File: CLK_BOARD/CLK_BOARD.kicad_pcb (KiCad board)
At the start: 4 copper layers, 46.5 x 38.7 mm, 79 parts, among them J1 PWR, J2 OUT_50M_1, J3 OUT_50M_2, J4 OUT_50M_3, J5 CTRL, J6 OUT_100M_3, J7 OUT_100M_2, J8 OUT_100M_1, U1 TPS7A9101DSKR, U2 LMK00804BQWRGTRQ1, U3 LMK00804BQWRGTRQ1, U4 SN74LVC1G74DCUR, X1 TB612-100.0M

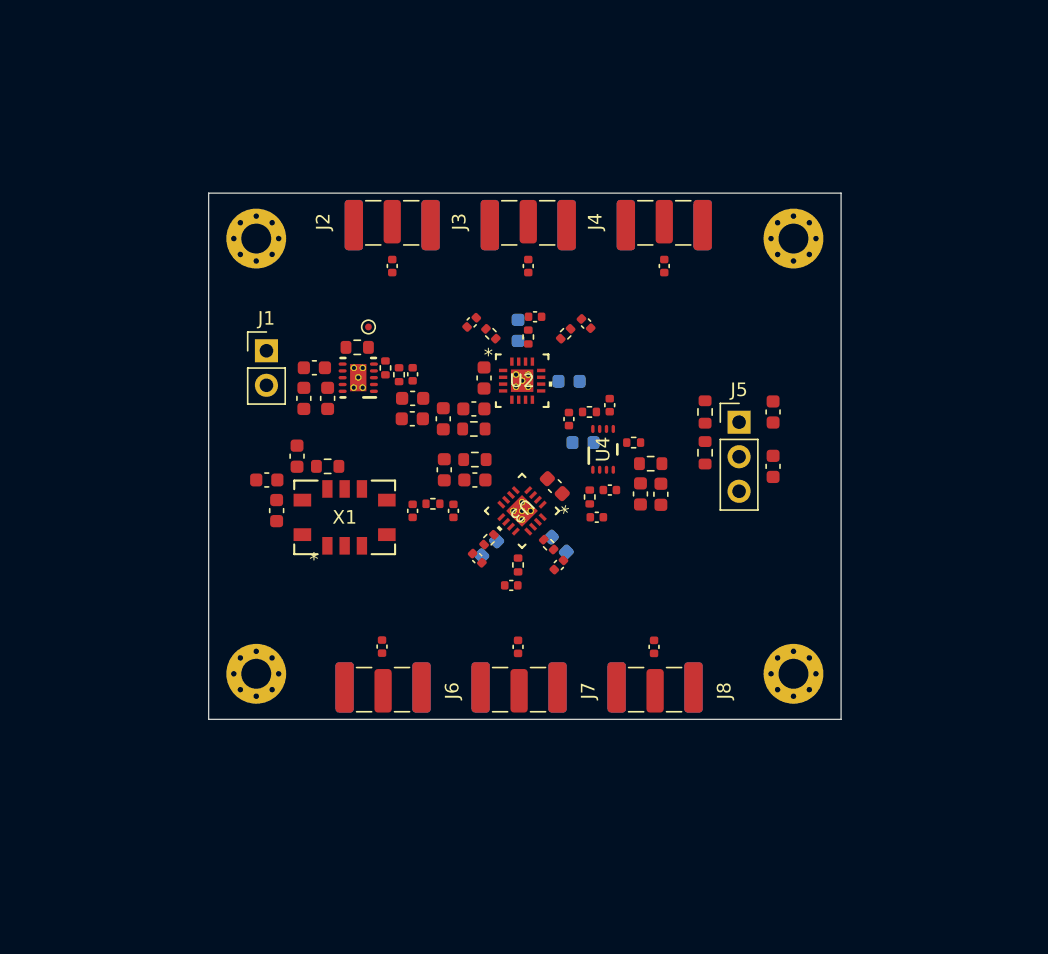
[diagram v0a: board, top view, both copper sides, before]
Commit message: component placement semi-final, and most tracks routed
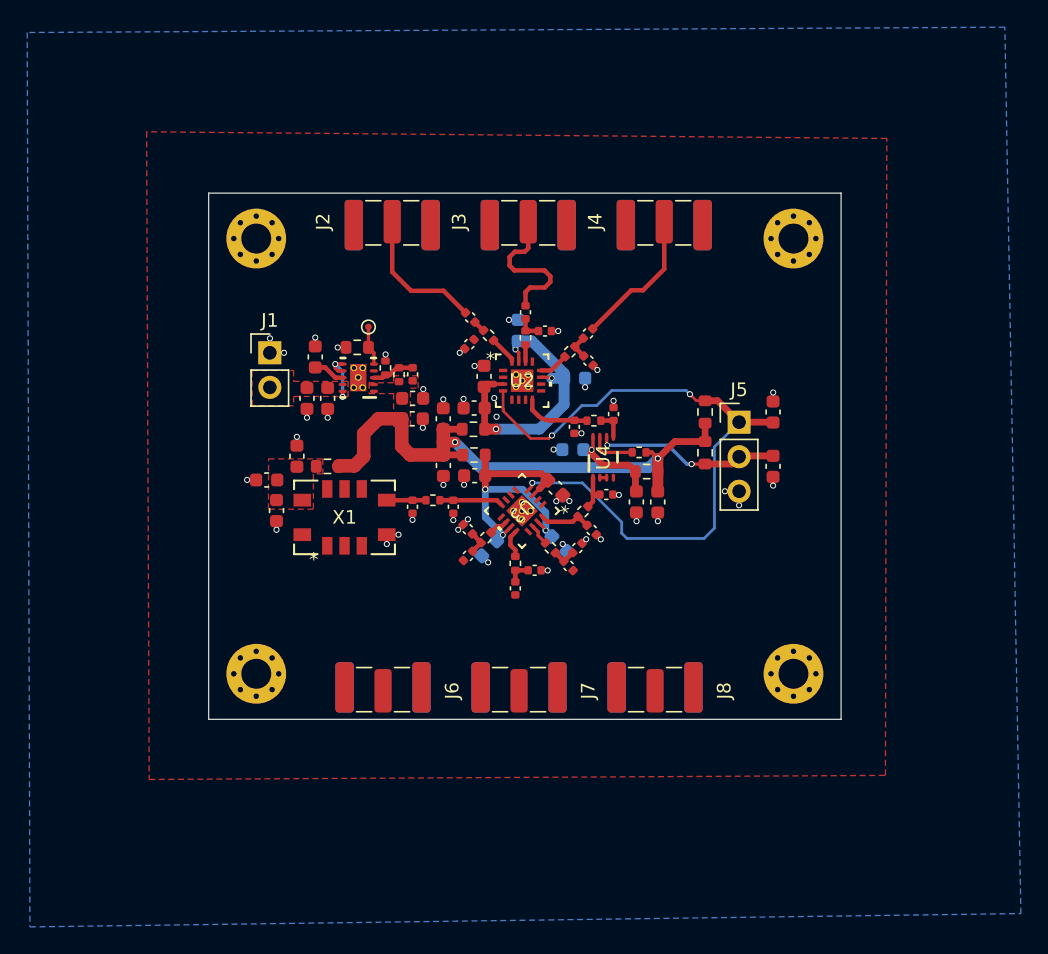
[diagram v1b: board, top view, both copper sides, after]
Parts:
- moved C35 9.19 mm to (131.1, 87.3), turned to -135 degrees
- moved C37 8.66 mm to (138.5, 88.1), turned to -45 degrees
- moved C28 7.49 mm to (139.9, 71.0), turned to -135 degrees
- moved C15 6.87 mm to (131.2, 69.8), turned to -45 degrees
- moved C36 4.30 mm to (134.6, 89.7)
- moved C22 3.41 mm to (135.3, 69.4)
- moved C29 2.73 mm to (139.9, 73.0)
- moved C32 2.24 mm to (131.1, 85.4), turned to 135 degrees
- moved C33 2.05 mm to (136.0, 88.4), turned to 0 degrees
- moved C34 1.85 mm to (139.1, 86.8), turned to 45 degrees
- moved C16 1.61 mm to (131.2, 71.8)
- moved R11 1.36 mm to (138.6, 72.3)
- moved C23 1.28 mm to (136.7, 70.8)
- moved R9 1.18 mm to (139.5, 84.1), turned to 45 degrees
- moved C24 1.01 mm to (140.2, 85.4), turned to -45 degrees
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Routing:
- net /nMUTE: track 0.00 -> 49.7 mm, vias 0 -> 3
- net +3V3: track 0.00 -> 42.8 mm, vias 0 -> 2
- net Net-(U3-VDD): track 0.00 -> 22.4 mm, vias 0 -> 3
- net Net-(U2-VDD): track 0.00 -> 21.3 mm, vias 0 -> 3
- net /nRST: track 0.00 -> 13.7 mm, vias 0 -> 2
- net Net-(J3-In): track 0.00 -> 11.1 mm
- net Net-(J4-In): track 0.00 -> 10.6 mm
- net Net-(J2-In): track 0.00 -> 10.3 mm
- net Net-(U4-VCC): track 0.00 -> 7.15 mm, vias 0 -> 1
- net Net-(U2-LVCMOS_CLK): track 0.00 -> 5.04 mm
- net /OSC_OUT: track 0.00 -> 4.65 mm
- net Net-(J1-Pin_2): track 0.00 -> 4.50 mm, vias 0 -> 2
- net Net-(U3-Q0): track 0.00 -> 3.83 mm
- net Net-(U4-PRE_N): track 0.00 -> 3.45 mm
- net Net-(U1-FB): track 0.00 -> 3.15 mm
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- added copper zone on F.Cu, net +3V3
- added copper zone on B.Cu, net GND
- added copper zone on F.Cu, net GND
- added copper zone on In1.Cu, net GND
- added copper zone on In2.Cu, net GND
- added copper zone on F.Cu, net Net-(J1-Pin_2)
- added copper zone on F.Cu, net Net-(X1-VCC)

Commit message: added via fencing around the edge and added epic silkscreen image
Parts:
- added G***: LOGO, Snapeda:beacon_test, B.Cu at (135.3, 87.7)
- moved J7 0.43 mm to (135.2, 97.2)
- moved J8 0.43 mm to (145.2, 97.2)
- moved J6 0.42 mm to (125.2, 97.2)
- moved J2 0.25 mm to (125.2, 62.8)
- moved J3 0.25 mm to (135.2, 62.8)
- moved J4 0.25 mm to (145.2, 62.8)
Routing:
- net Net-(J3-In): track 11.1 -> 0.00 mm
- net Net-(J4-In): track 10.6 -> 0.00 mm
- net Net-(J2-In): track 10.3 -> 0.00 mm
- net GND: vias 47 -> 103

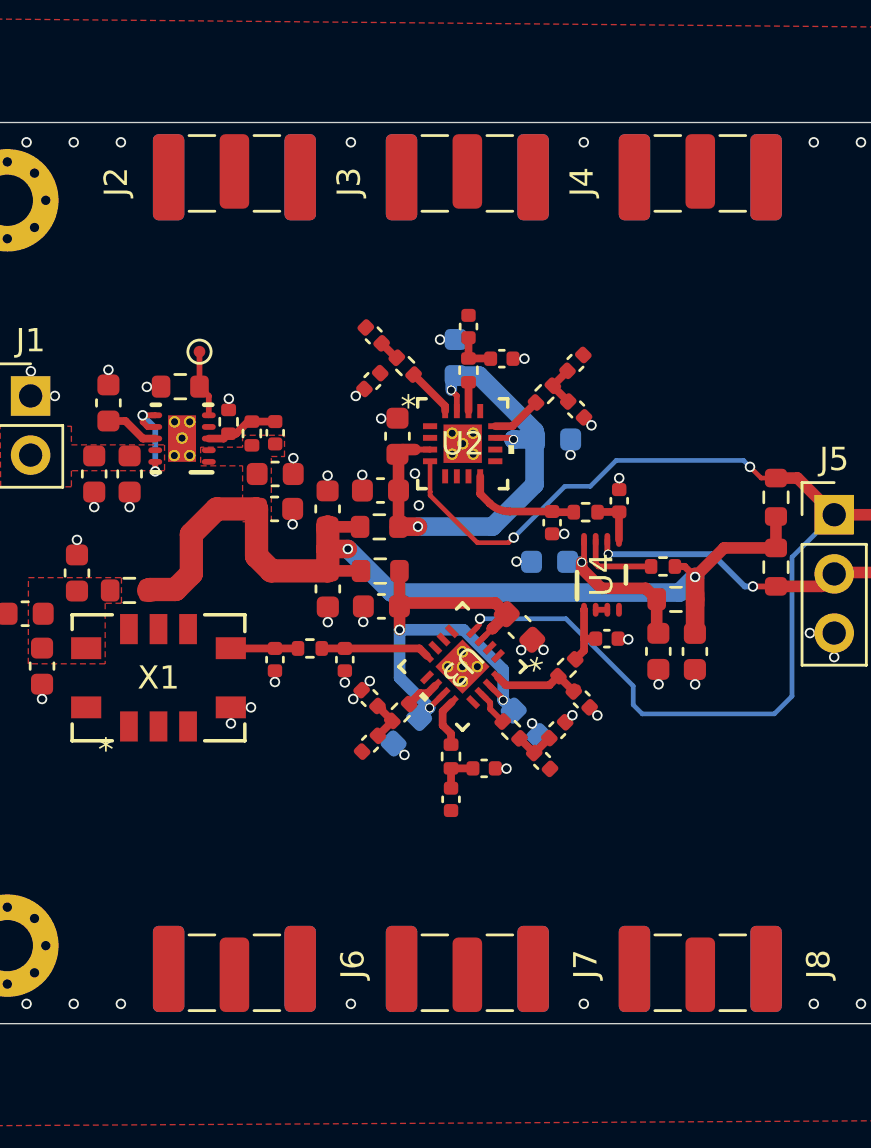
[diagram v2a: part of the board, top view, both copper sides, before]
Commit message: almost finished with layout, need stiching vias then it's finished
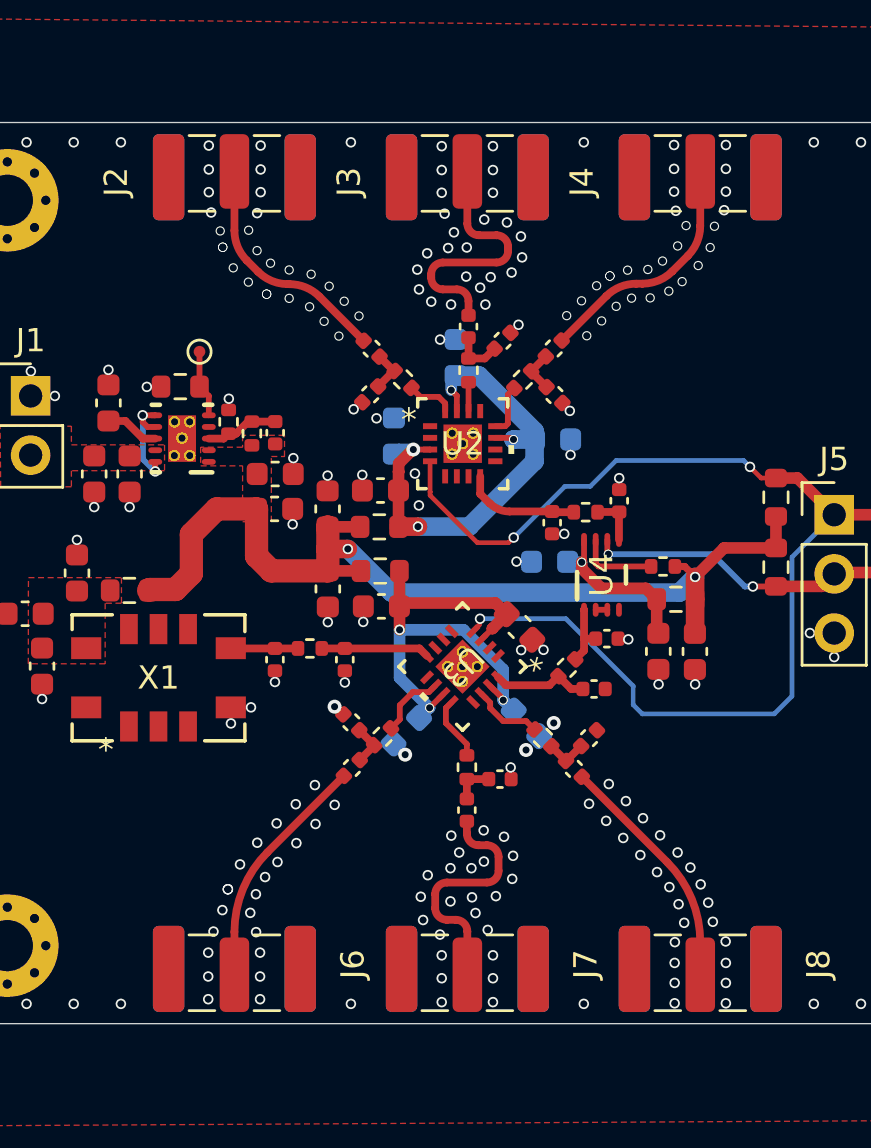
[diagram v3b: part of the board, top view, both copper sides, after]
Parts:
- C11: moved to B.Cu
- moved R16 1.41 mm to (138.5, 87.1)
- moved C37 1.41 mm to (139.8, 88.4)
- moved C34 1.41 mm to (140.5, 87.1)
- moved C35 1.30 mm to (130.3, 88.4)
- moved C32 1.30 mm to (130.3, 86.4)
- moved R14 1.30 mm to (131.6, 87.0)
- moved C29 1.12 mm to (139.0, 72.4)
- moved C28 1.12 mm to (139.0, 70.4)
- moved R11 1.12 mm to (137.6, 71.7)
- moved C33 0.82 mm to (136.7, 88.9)
- moved C36 0.82 mm to (135.2, 90.2)
- moved R15 0.82 mm to (135.2, 88.3)
- moved C23 0.77 mm to (136.8, 70.0), turned to 45 degrees
- moved C24 0.69 mm to (140.7, 85.0), turned to 0 degrees
- moved C15 0.58 mm to (131.1, 70.4)
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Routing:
- net Net-(J3-In): track 0.00 -> 11.5 mm
- net Net-(J7-In): track 0.00 -> 10.6 mm
- net Net-(J4-In): track 0.00 -> 10.5 mm
- net Net-(J8-In): track 0.00 -> 10.4 mm
- net Net-(J6-In): track 0.00 -> 10.3 mm
- net Net-(J2-In): track 0.00 -> 10.2 mm
- net Net-(U3-Q3): track 1.45 -> 3.02 mm
- net Net-(U3-Q1): track 1.57 -> 3.05 mm
- net Net-(C15-Pad2): track 0.91 -> 1.89 mm
- net Net-(U3-Q2): track 2.14 -> 2.76 mm
- net Net-(U2-VDD): vias 3 -> 4
- net GND: vias 103 -> 252
